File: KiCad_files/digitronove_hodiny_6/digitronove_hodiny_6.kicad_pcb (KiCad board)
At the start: 2 copper layers, 149 x 92 mm, 55 parts, among them J1 Nixie_CATHODES, J2 Nixie_ANODES, J3 Conn_01x05, J4 Conn_01x05, J5 Conn_01x02, Q1 MPSA42, Q10 MPSA42, Q2 MPSA42, Q3 MPSA42, Q4 MPSA42, Q5 MPSA42, Q6 MPSA42, Q7 MPSA42, Q8 MPSA42, Q9 MPSA42, U1 WeMos_D1_mini, U10 74HC595, U12 AMS1117-3.3, U2 74HC595, U3 74HC595, U4 TLP627, U5 TLP627, U6 TLP627, U7 TLP627, U8 TLP627, U9 TLP627

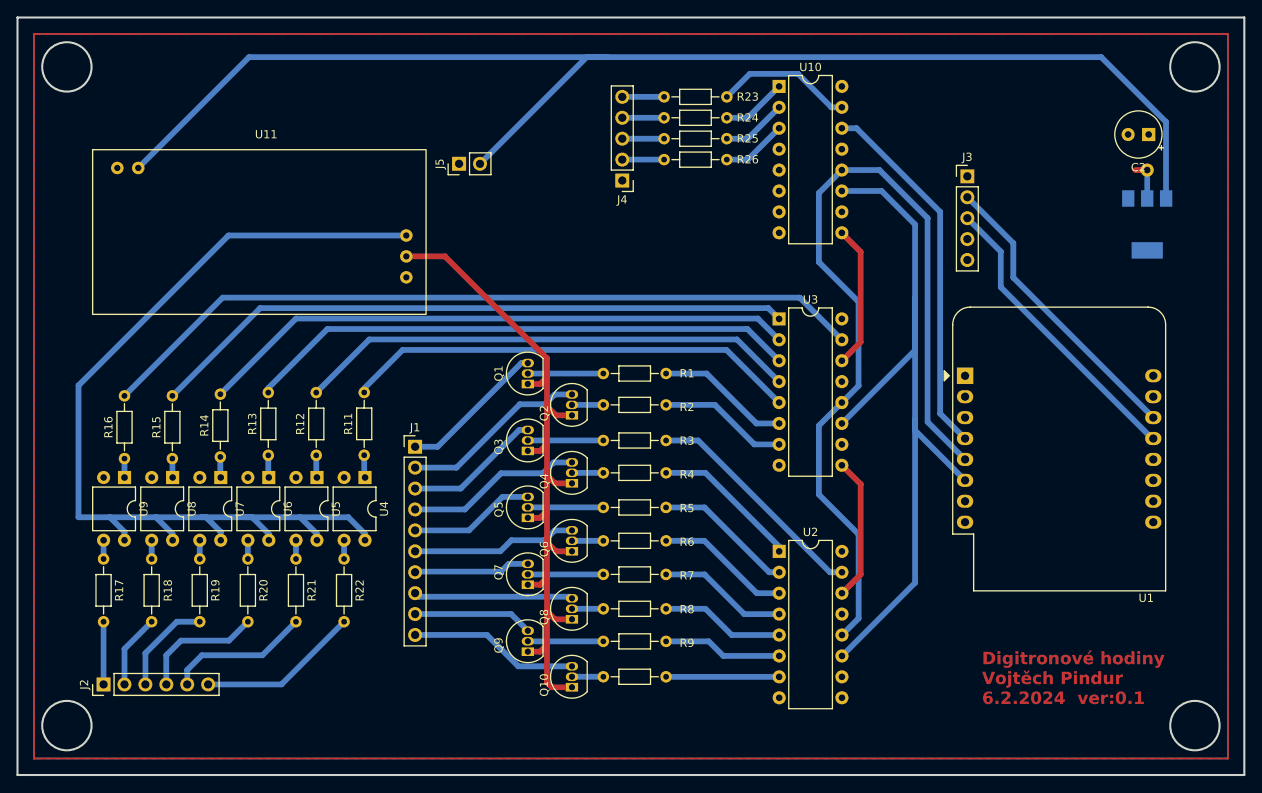
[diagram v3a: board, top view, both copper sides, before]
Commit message: Created resources directory, EDA files update.
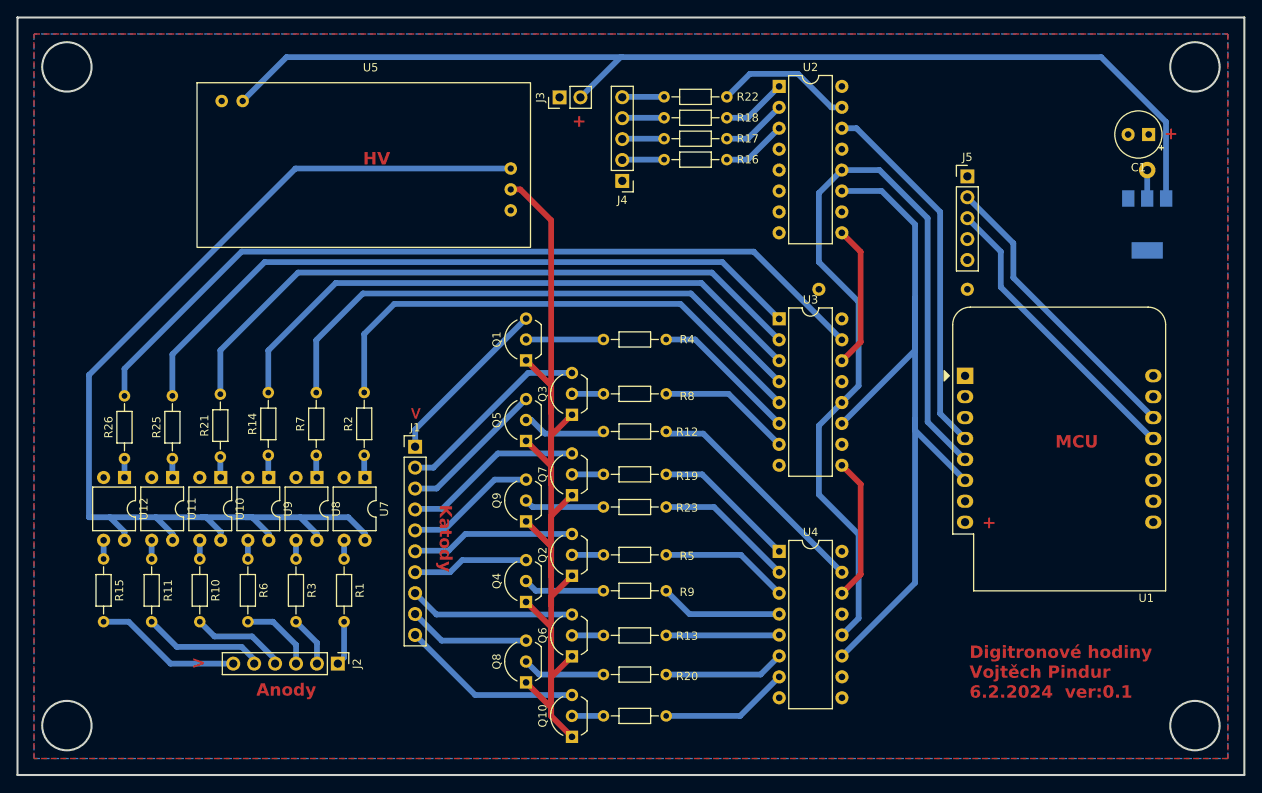
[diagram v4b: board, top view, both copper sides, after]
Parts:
- added ?: , , F.Cu at (195.3, 64.0)
- added ?: , , F.Cu at (213.4, 64.0)
- J1: value Nixie_CATHODES -> Conn_01x10
- J2: value Nixie_ANODES -> Conn_01x06
- Q1, Q10: footprint Package_TO_SOT_THT:TO-92_Inline -> Package_TO_SOT_THT:TO-92_Inline_Wide
- Q2: renamed from Q6; footprint Package_TO_SOT_THT:TO-92_Inline -> Package_TO_SOT_THT:TO-92_Inline_Wide
- Q3: renamed from Q2; footprint Package_TO_SOT_THT:TO-92_Inline -> Package_TO_SOT_THT:TO-92_Inline_Wide
- Q4: renamed from Q7; footprint Package_TO_SOT_THT:TO-92_Inline -> Package_TO_SOT_THT:TO-92_Inline_Wide
- Q5: renamed from Q3; footprint Package_TO_SOT_THT:TO-92_Inline -> Package_TO_SOT_THT:TO-92_Inline_Wide
- Q6: renamed from Q8; footprint Package_TO_SOT_THT:TO-92_Inline -> Package_TO_SOT_THT:TO-92_Inline_Wide
- Q7: renamed from Q4; footprint Package_TO_SOT_THT:TO-92_Inline -> Package_TO_SOT_THT:TO-92_Inline_Wide
- Q8: renamed from Q9; footprint Package_TO_SOT_THT:TO-92_Inline -> Package_TO_SOT_THT:TO-92_Inline_Wide
- Q9: renamed from Q5; footprint Package_TO_SOT_THT:TO-92_Inline -> Package_TO_SOT_THT:TO-92_Inline_Wide
- moved J2 28.6 mm to (136.9, 109.5), turned to -90 degrees
- moved U5 15.1 mm to (119.8, 58.9)
- moved J3 14.6 mm to (163.8, 40.7)
- moved Q10 6.02 mm to (165.3, 118.4)
- moved R24 4.75 mm to (169.2, 115.8)
- moved Q6 4.50 mm to (165.3, 108.6)
- moved R4 4.14 mm to (169.2, 70.1)
- moved R20 4.03 mm to (169.2, 110.8)
- moved Q8 3.74 mm to (159.8, 111.8)
- moved R13 3.23 mm to (169.2, 106.0)
- moved Q2 2.98 mm to (165.3, 98.8)
- moved Q1 2.87 mm to (159.8, 72.6)
- moved Q4 2.10 mm to (159.8, 102.0)
- moved R9 1.99 mm to (169.2, 100.6)
- moved R5 1.71 mm to (169.2, 96.3)
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- renumbered C2 to C1, J5 to J3, J3 to J5, R22 to R1, R19 to R10, R18 to R11, R3 to R12, R8 to R13, R13 to R14, R17 to R15, R26 to R16, R25 to R17, R24 to R18, R4 to R19, R11 to R2, R9 to R20, R14 to R21, R23 to R22, R5 to R23, R10 to R24, R15 to R25, R16 to R26, R21 to R3, R1 to R4, R6 to R5, R20 to R6, R12 to R7, R2 to R8, R7 to R9, U7 to U10, U8 to U11, U9 to U12, U10 to U2, U2 to U4, U11 to U5, U12 to U6, U4 to U7, U5 to U8, U6 to U9
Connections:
- R1 pad 2: Net-(J2-Pin_6) -> Net-(J2-Pin_1)
- R10 pad 2: Net-(J2-Pin_3) -> Net-(J2-Pin_4)
- R11 pad 2: Net-(J2-Pin_2) -> Net-(J2-Pin_5)
- R15 pad 2: Net-(J2-Pin_1) -> Net-(J2-Pin_6)
- R3 pad 2: Net-(J2-Pin_5) -> Net-(J2-Pin_2)
- R6 pad 2: Net-(J2-Pin_4) -> Net-(J2-Pin_3)
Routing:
- net GND_CAT: track 92.0 -> 132.1 mm
- net VCC: track 163.8 -> 134.0 mm
- net HV_ANODE: track 119.0 -> 133.3 mm
- net ANODE_5: track 55.5 -> 64.0 mm
- net ANODE_4: track 61.0 -> 69.4 mm
- net ANODE_2: track 72.7 -> 80.5 mm
- net ANODE_1: track 78.6 -> 86.2 mm
- net ANODE_3: track 67.1 -> 74.5 mm
- net ANODE_0: track 94.2 -> 100.7 mm
- net Net-(J2-Pin_4): track 15.1 -> 11.6 mm
- net CAT_0: track 17.9 -> 21.1 mm
- net Net-(J2-Pin_2): track 8.98 -> 6.15 mm
- net Net-(J2-Pin_3): track 12.0 -> 9.30 mm
- net Net-(J2-Pin_5): track 17.4 -> 14.9 mm
- net Net-(J2-Pin_1): track 7.62 -> 5.40 mm
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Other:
- board text added: "+"
- board text added: ">"
- board text added: "Anody"
- board text added: "HV"
- board text added: "Katody"
- board text added: "MCU"

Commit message: PCB Design update
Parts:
- added ?: , , F.Cu at (104.0, 37.0)
- added ?: , , F.Cu at (241.0, 117.0)
- added ?: , , F.Cu at (104.0, 117.0)
- added ?: , , F.Cu at (241.0, 37.0)
- added C2: C_Polarized, Capacitor_THT:CP_Radial_Tantal_D5.5mm_P2.50mm, F.Cu at (239.1, 45.2)
- renumbered J2 to J1, J1 to J2, Q3 to Q2, Q5 to Q3, Q7 to Q4, Q9 to Q5, Q2 to Q6, Q4 to Q7, Q6 to Q8, Q8 to Q9, R4 to R1, R24 to R10, R2 to R11, R7 to R12, R14 to R13, R21 to R14, R25 to R15, R26 to R16, R1 to R17, R3 to R18, R6 to R19, R8 to R2, R10 to R20, R11 to R21, R15 to R22, R16 to R23, R17 to R24, R18 to R25, R22 to R26, R12 to R3, R19 to R4, R23 to R5, R5 to R6, R9 to R7, R13 to R8, R20 to R9, U6 to U5, U5 to U6
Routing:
- net VCC: track 134.0 -> 136.2 mm
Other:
- outline, holes or cut-outs redrawn
- board text added: "-"
- board text added: "D"
- board text added: "Digitronové hodiny Vojtěch Pindur 19.2.2024 ver:0.1"
- board text removed: "Digitronové hodiny Vojtěch Pindur 6.2.2024 ver:0.1"
